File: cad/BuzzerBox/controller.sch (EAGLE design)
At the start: 120 parts, among them Q1 BSS138, Q2 BSS138, T1 BC849, T10 BC849, T2 BC849, T3 BC849, T4 BC849, T5 BC849, T6 BC849, T7 BC849, T8 BC849, T9 BC849, U1 ATMEGA328P-AU, Y1 16MHz

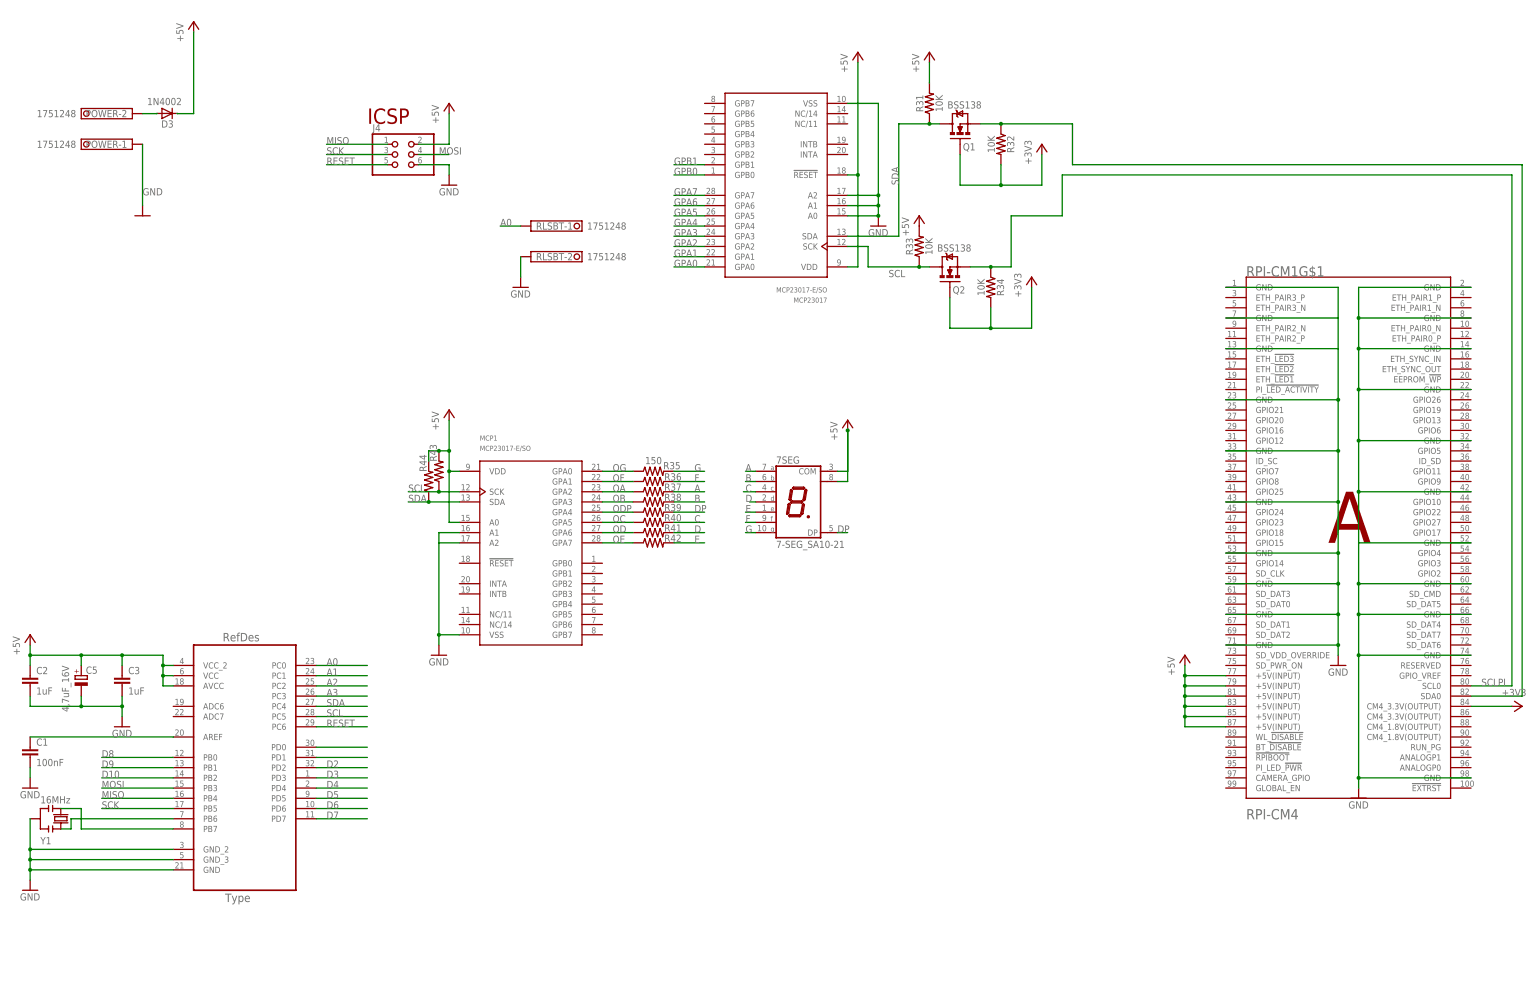
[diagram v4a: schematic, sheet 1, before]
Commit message: Add USB port
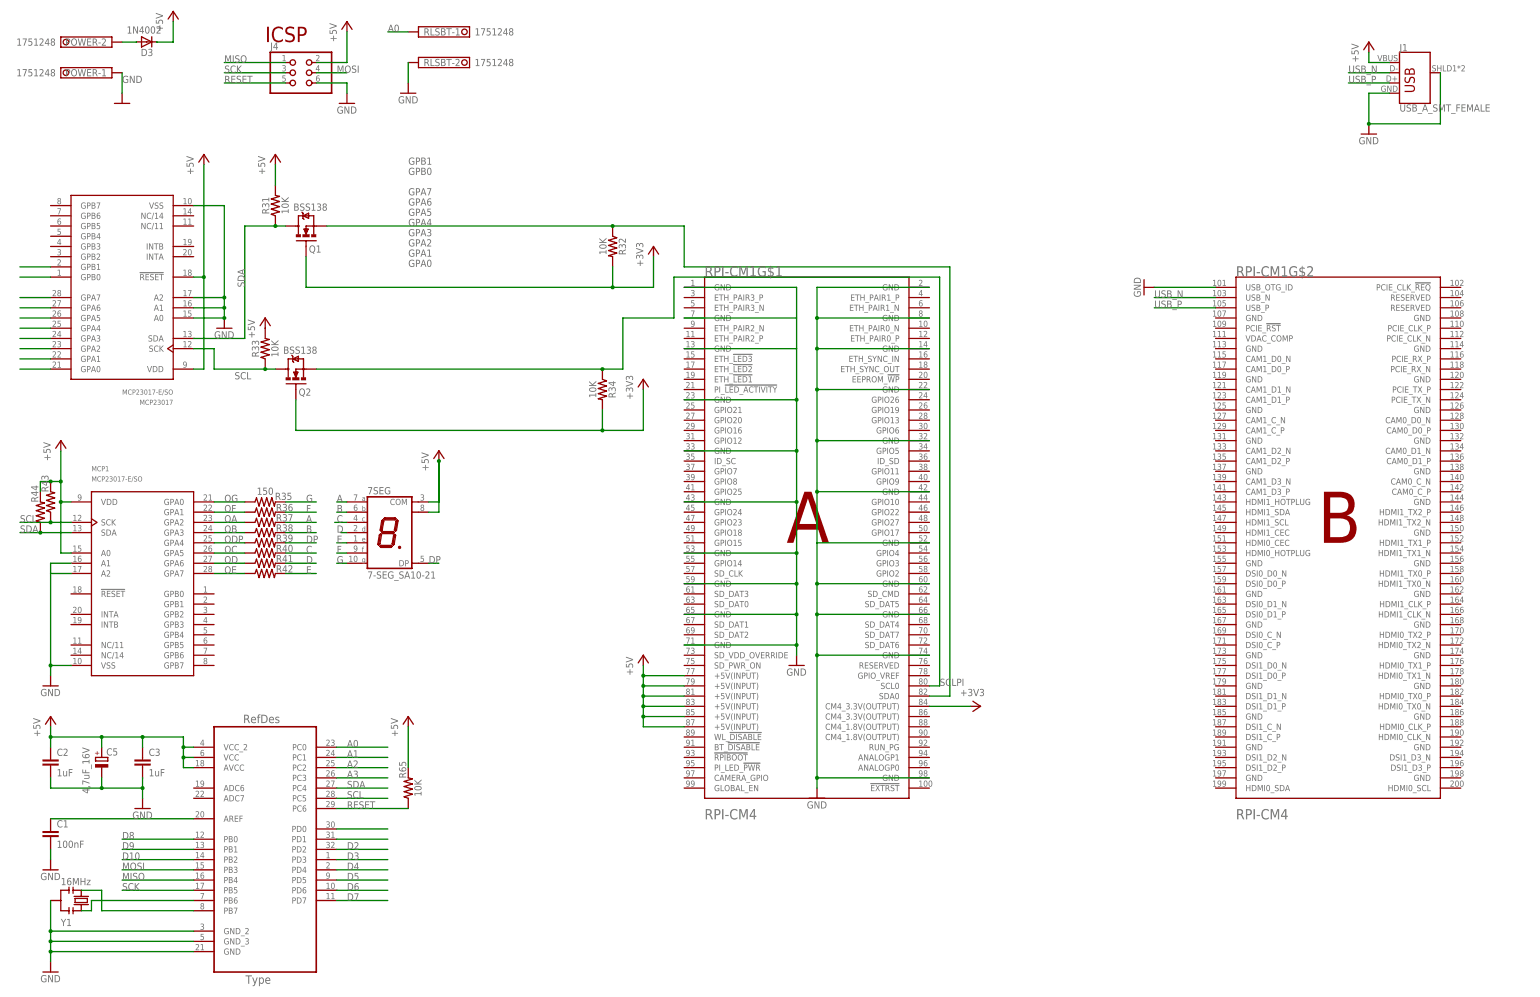
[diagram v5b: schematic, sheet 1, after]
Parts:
- added J1: USB_A_SMT_FEMALE, SparkFun-Connectors:USB_A_SMT_FEMALE
- added R65: 10K, SparkFun-Resistors:RESISTOR0805
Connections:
- new net USB_N: J1.D-, RPI-CM1G$2.USB_N
- new net USB_P: J1.D+, RPI-CM1G$2.USB_P
- net +5V: now also J1.VBUS, R65.2
- net GND: now also J1.GND, J1.SHIELD, RPI-CM1G$2.USB_OTG_ID
- net RESET: now also R65.1
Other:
- moved on the sheet: 7SEG, C1, C2, C3, C5, D3, J4, MCP1, MCP23017, POWER-1, POWER-2, Q1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

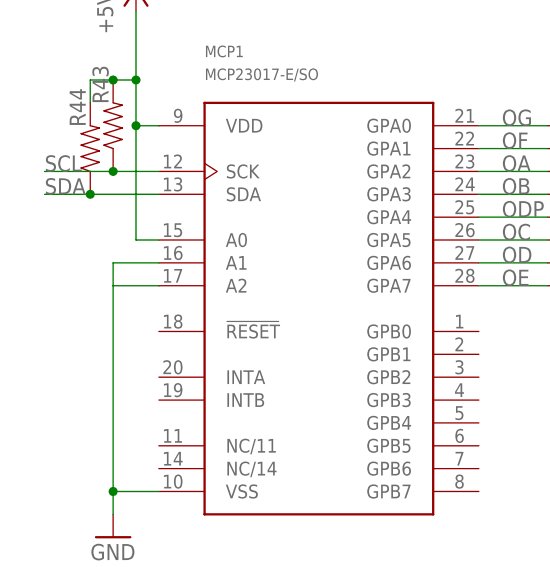
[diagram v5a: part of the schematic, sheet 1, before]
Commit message: Fix missig Reset pin voltage on I2c-expander
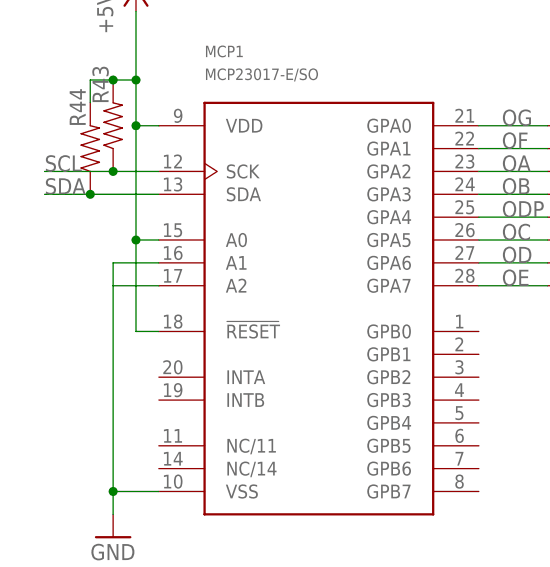
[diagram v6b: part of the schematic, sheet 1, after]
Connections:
- net +5V: now also MCP1.!RESET
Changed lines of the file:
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@@
 <wire x1="-71.12" y1="88.9" x2="-68.58" y2="88.9" width="0.1524" layer="91"/>
 <junction x="-68.58" y="88.9"/>
+<wire x1="-66.04" y1="71.12" x2="-66.04" y2="60.96" width="0.1524" layer="91"/>
+<junction x="-66.04" y="71.12"/>
+<pinref part="MCP1" gate="G$1" pin="!RESET"/>
+<wire x1="-66.04" y1="60.96" x2="-63.5" y2="60.96" width="0.1524" layer="91"/>
 </segment>
 <segment>
